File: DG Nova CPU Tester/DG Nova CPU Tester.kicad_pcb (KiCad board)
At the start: 2 copper layers, 414.8 x 131.4 mm, 115 parts, among them J1 Front Panel Socket - Backside, J10 Programmed I/O, J11 CPU Option Inputs, J12 Data Channel, J13 Program Interrupt, J14 System Control, J15 Slot_02x50_Odd_Even, J16 Slot_02x50_Odd_Even, J17 CPU Option Outputs, J18 MEM Control Outputs, J19 Logic 8 CH, J20 Logic 8 CH, J21 Arduino Anolog Pins, J22 Arduino Digital Pins, J23 Arduino Digital Pins, J4 ATX-24, J5 Front Panel Card Edge, J6 MBO, J7 MEM, J8 Data Channel, J9 Front Panel Controls, SW1 SW_Push, U1 74HC14, U2 Pico

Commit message: All Board Signal Traces Pulled Up
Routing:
- net ~{MB CLEAR}: track 3.43 -> 163.2 mm, vias 0 -> 1
- net ~{EXT LOAD}: track 3.56 -> 162.0 mm
- net ~{DATA14}: track 3.43 -> 161.6 mm, vias 0 -> 1
- net ~{DRIVE IO}: track 3.43 -> 160.7 mm, vias 0 -> 1
- net ~{MEM1}: track 19.7 -> 176.2 mm, vias 0 -> 1
- net MB LOAD: track 2.92 -> 159.4 mm
- net ~{DATA2}: track 3.43 -> 159.7 mm
- net ~{MEM3}: track 19.7 -> 175.8 mm
- net ~{DS2}: track 3.43 -> 159.5 mm
- net ~{DATA13}: track 3.43 -> 159.0 mm, vias 0 -> 1
- net ~{FETCH}: track 20.2 -> 175.5 mm
- net ~{DATA11}: track 3.43 -> 158.6 mm, vias 0 -> 1
- net ~{DATA8}: track 3.43 -> 158.5 mm, vias 0 -> 1
- net DATOB: track 2.92 -> 158.0 mm
- net ~{MEM14}: track 27.0 -> 181.7 mm
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
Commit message: All Top Signal Traces Pulled Down
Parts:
- moved J21 417.4 mm to (-172.0, 63.0)
- moved J23 417.4 mm to (-122.2, 106.6)
- moved XA1 417.4 mm to (-80.5, 58.2)
- moved J22 417.4 mm to (-138.9, 106.6)
- moved SW1 406.9 mm to (-124.3, -57.2)
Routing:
- net ~{WAS JSR}: track 82.0 -> 221.1 mm, vias 0 -> 2
- net ~{FETCH}: track 175.5 -> 225.5 mm, vias 0 -> 1
- net ~{CARRY}: track 100.7 -> 150.6 mm
- net ~{RUN}: track 113.9 -> 163.8 mm, vias 0 -> 1
- net ~{MBO6}: track 171.8 -> 219.7 mm
- net ~{EXEC}: track 95.3 -> 142.8 mm, vias 0 -> 1
- net ~{DEFER}: track 101.7 -> 149.2 mm, vias 0 -> 1
- net ~{ION}: track 115.4 -> 161.3 mm, vias 0 -> 1
- net ~{MBO3}: track 156.9 -> 201.7 mm
- net ~{MEM5}: track 168.0 -> 212.7 mm
- net ~{MBO12}: track 160.9 -> 204.7 mm
- net ~{MEM10}: track 160.9 -> 204.5 mm
- net ~{MEM1}: track 176.2 -> 219.7 mm
- net ~{MEM7}: track 170.7 -> 214.1 mm
- net ~{MEM0}: track 161.6 -> 204.8 mm
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
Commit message: Progress!
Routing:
- net +5V: track 60.8 -> 532.7 mm
- net GND: track 27.7 -> 472.6 mm
- net ~{READ2}: track 177.6 -> 438.9 mm, vias 0 -> 3
- net ~{DATA1}: track 165.9 -> 426.2 mm
- net ~{MEM0}: track 204.8 -> 425.0 mm
- net MB LOAD: track 184.1 -> 393.2 mm
- net ~{MEM1}: track 219.7 -> 425.6 mm
- net ~{DATA9}: track 165.6 -> 362.8 mm
- net ~{READ1}: track 167.1 -> 359.8 mm, vias 0 -> 2
- net ~{MEM3}: track 218.2 -> 407.5 mm
- net ~{DATA4}: track 167.7 -> 356.8 mm
- net ~{DATA13}: track 180.4 -> 366.0 mm
- net ~{DATA15}: track 183.7 -> 367.3 mm
- net ~{DATA0}: track 181.6 -> 364.1 mm
- net ~{DATA12}: track 166.3 -> 342.7 mm
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
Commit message: ALL Backplane Sockets Connected
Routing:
- net ~{DATA6}: track 104.6 -> 431.7 mm, vias 0 -> 1
- net ~{DRIVE IO}: track 186.8 -> 461.1 mm, vias 1 -> 0
- net ~{MB CLEAR}: track 185.0 -> 455.3 mm, vias 1 -> 0
- net ~{DATA10}: track 164.5 -> 422.0 mm, vias 0 -> 1
- net ~{MBO0}: track 161.4 -> 411.9 mm
- net ~{MEM14}: track 214.4 -> 457.0 mm
- net ~{MBO1}: track 207.5 -> 448.9 mm
- net ~{DATA2}: track 183.4 -> 397.6 mm, vias 0 -> 1
- net CLR: track 184.0 -> 389.7 mm, vias 0 -> 1
- net ~{DATA3}: track 166.9 -> 367.6 mm, vias 0 -> 1
- net ~{MEM12}: track 207.4 -> 401.9 mm, vias 1 -> 2
- net ~{MEM13}: track 196.5 -> 387.5 mm, vias 0 -> 1
- net ~{MSKO}: track 176.6 -> 359.5 mm
- net ~{MBO13}: track 208.9 -> 391.2 mm, vias 0 -> 1
- net ~{READ IO}: track 168.1 -> 348.6 mm, vias 0 -> 1
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
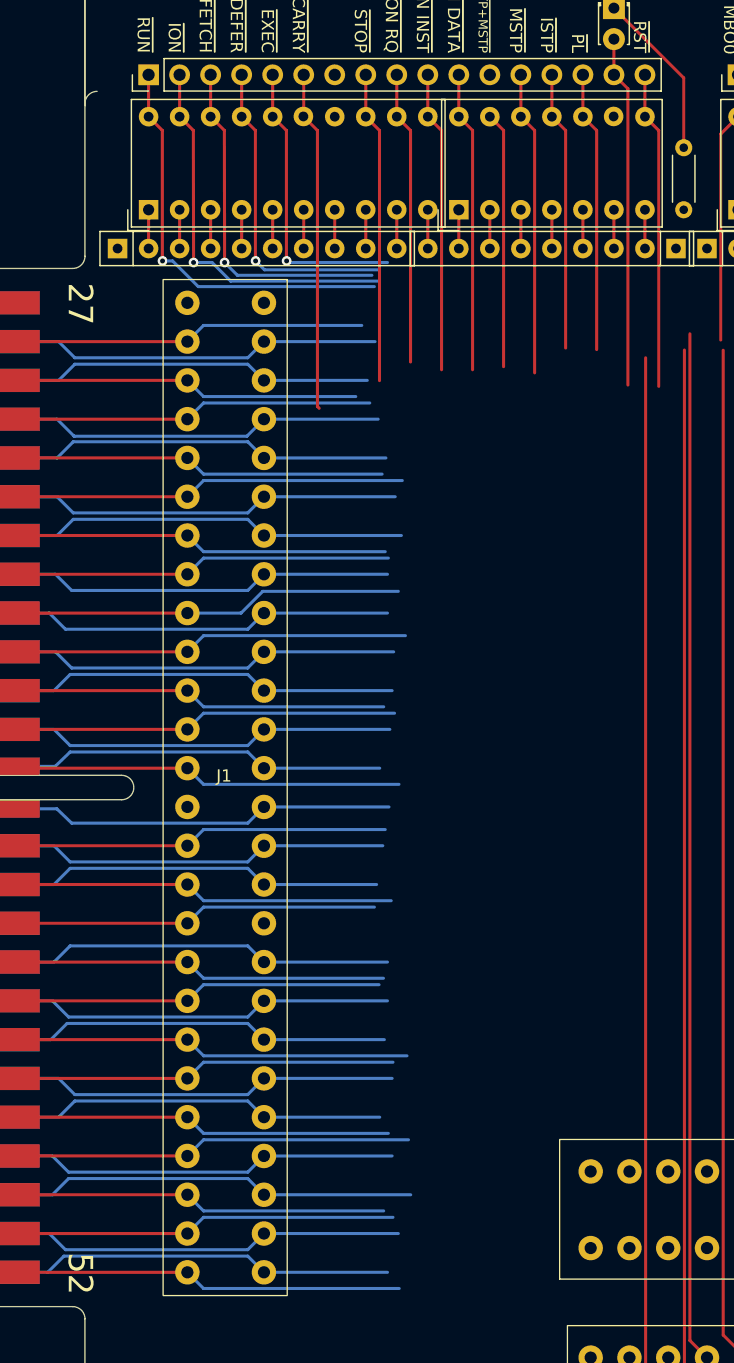
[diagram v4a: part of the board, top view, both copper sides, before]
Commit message: All Front Panel Control Signals
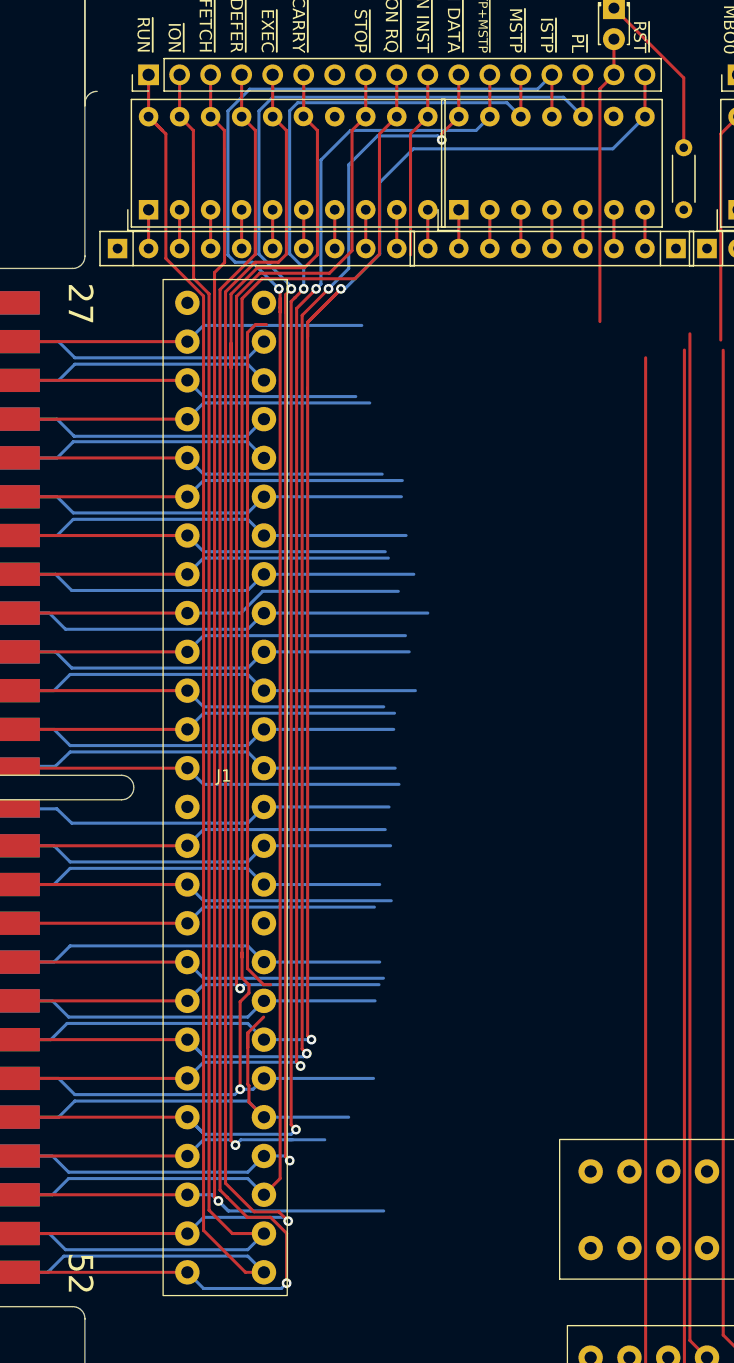
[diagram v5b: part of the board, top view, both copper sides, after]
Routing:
- net ~{ISTP}: track 134.3 -> 223.7 mm, vias 0 -> 1
- net ~{PL}: track 129.6 -> 218.1 mm, vias 0 -> 2
- net ~{MSTP}: track 137.2 -> 214.5 mm, vias 0 -> 2
- net ~{RST}: track 145.0 -> 219.1 mm, vias 0 -> 2
- net ~{DEFER}: track 149.2 -> 219.9 mm
- net ~{EXEC}: track 142.8 -> 211.1 mm
- net ~{CON RQ}: track 137.8 -> 206.0 mm, vias 0 -> 1
- net ~{FETCH}: track 225.5 -> 292.2 mm
- net ~{CONT+ISTP+MSTP}: track 130.4 -> 195.9 mm, vias 0 -> 2
- net ~{CARRY}: track 150.6 -> 212.0 mm, vias 0 -> 1
- net ~{RUN}: track 163.8 -> 224.1 mm, vias 1 -> 0
- net ~{CON DATA}: track 144.6 -> 203.0 mm, vias 0 -> 3
- net ~{STOP}: track 131.9 -> 189.3 mm, vias 0 -> 1
- net ~{ION}: track 161.3 -> 218.0 mm, vias 1 -> 0
- net ~{CON INST}: track 136.8 -> 191.8 mm
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
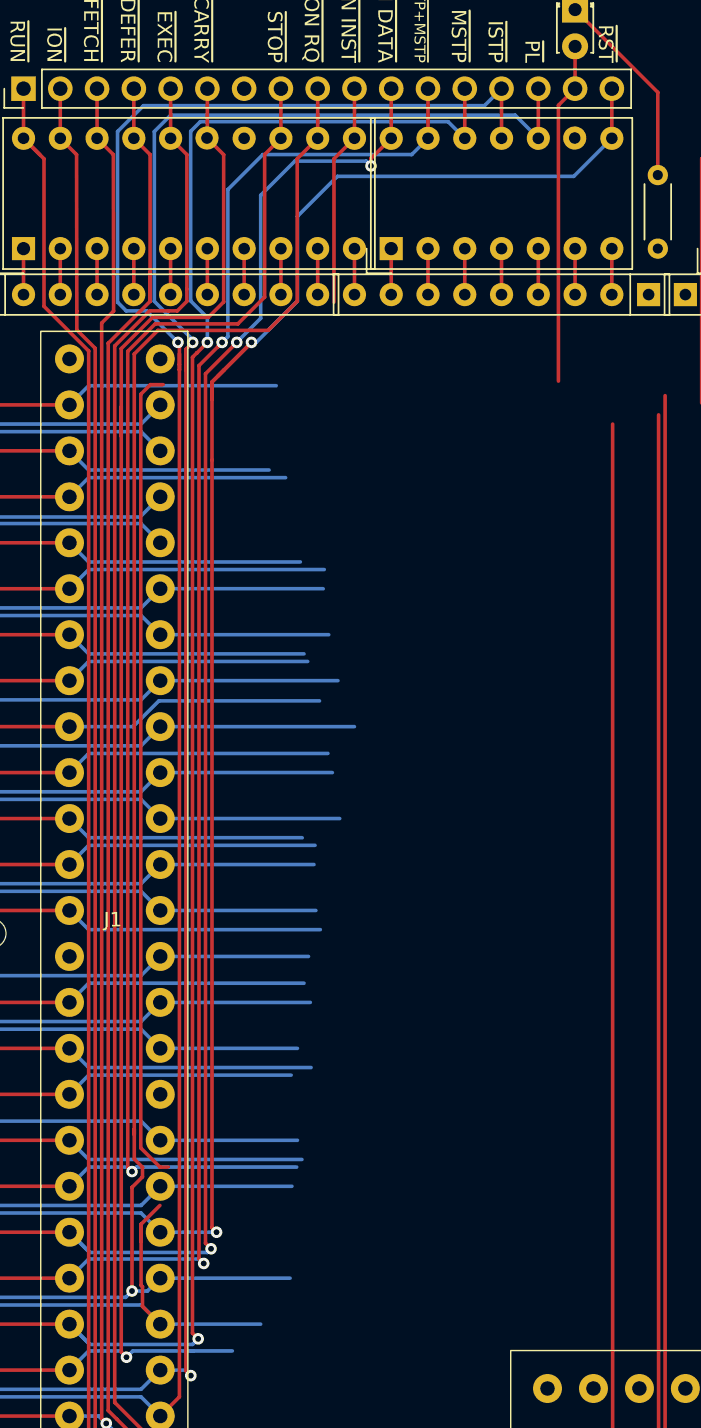
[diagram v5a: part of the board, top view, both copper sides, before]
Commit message: All Front Panel Control Signals 2
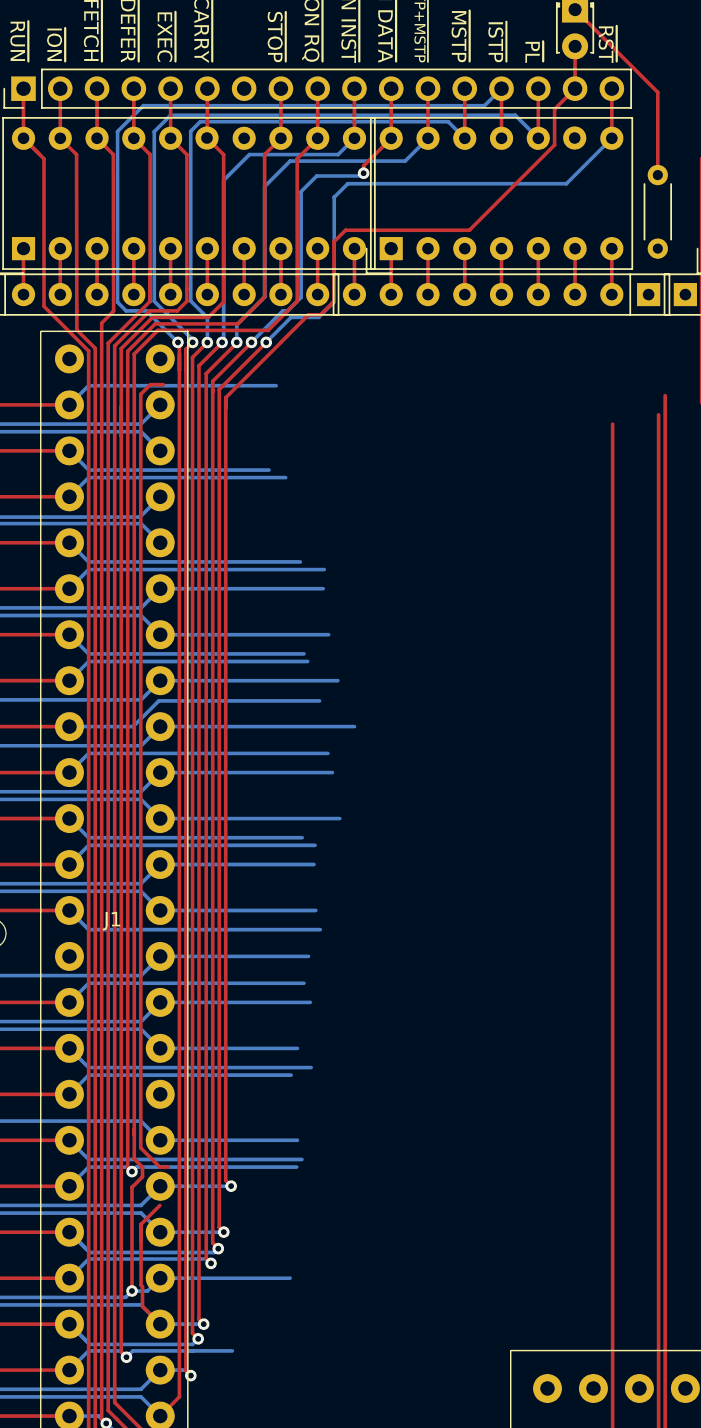
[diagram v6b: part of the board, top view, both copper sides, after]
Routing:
- net ~{CON INST}: track 191.8 -> 266.1 mm, vias 0 -> 2
- net RESTART ENABLE: track 136.6 -> 203.8 mm, vias 0 -> 1
- net ~{RST}: track 219.1 -> 213.9 mm
- net ~{CON DATA}: track 203.0 -> 201.8 mm
- net ~{CONT+ISTP+MSTP}: track 195.9 -> 194.8 mm

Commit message: Arduino Placement
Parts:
- moved J23 236.4 mm to (114.1, 104.4)
- moved XA1 236.4 mm to (155.8, 56.0)
- moved J21 236.4 mm to (64.4, 60.8)
- moved J22 236.4 mm to (97.4, 104.5)
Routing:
- net MEM OK: track 104.8 -> 446.6 mm, vias 0 -> 2
- net ~{MBO10}: track 212.2 -> 304.3 mm, vias 0 -> 2
- net ~{MBO8}: track 227.5 -> 308.7 mm, vias 2 -> 4
- net ~{FETCH}: track 292.2 -> 271.7 mm
- net ~{CARRY}: track 212.0 -> 197.4 mm
- net ~{STOP}: track 189.3 -> 177.8 mm
- net ~{MEM15}: track 234.4 -> 223.4 mm
- net ~{EXEC}: track 211.1 -> 201.6 mm
- net ~{RUN}: track 224.1 -> 214.9 mm
- net ~{MEM3}: track 407.5 -> 398.3 mm
- net ~{CON RQ}: track 206.0 -> 197.0 mm
- net ~{MEM7}: track 252.4 -> 243.5 mm
- net ~{MEM14}: track 448.6 -> 439.9 mm
- net ~{MEM5}: track 260.2 -> 251.8 mm
- net ~{MEM13}: track 387.5 -> 379.2 mm
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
